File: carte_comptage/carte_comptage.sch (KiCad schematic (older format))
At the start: 34 parts, among them U3.3V MC33269ST-3.3T3G

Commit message: carte comptage SWD
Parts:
- added Rboot0: 100k, Resistor_SMD:R_1206_3216Metric, symbol Device:R
- added SWD: micromatch, TE_7-215079-6, symbol 7-215079-6:7-215079-6
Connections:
- net labels added: BOOT0, BUCK_EN, NRST, SWCLK, SWDIO, UART_RX, UART_TX
- net labels removed: boot0, buck_en, nrst
- wire segments 105 -> 107
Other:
- moved on the sheet: Cb1, Cb2, Cbbs, Cbc1, Cbc2, Cbdc1, Cbdc2, Cbdc3, Cbss, Cdc1, Cdc2, Cdc3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

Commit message: debut xtal a finir
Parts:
- added Dstatus1: LED, symbol Device:LED
- added Rstatus1: R, Resistor_SMD:R_1206_3216Metric, symbol Device:R
- SWD1: renamed from SWD; symbol 7-215079-6:7-215079-6 -> carte_comptage-rescue:7-215079-6-7-215079-6
- U3.3V1: renamed from U3.3V; symbol MC33269ST-3.3T3G:MC33269ST-3.3T3G -> carte_comptage-rescue:MC33269ST-3.3T3G-MC33269ST-3.3T3G
- USB1: renamed from USB; symbol USB4105-GF-A:USB4105-GF-A -> carte_comptage-rescue:USB4105-GF-A-USB4105-GF-A
- renumbered Cbbs to Cbbs1, Cbss to Cbss1, Cdcr to Cdcr1, Crst to Crst1, Db to Db1, Dpow to Dpow1, Dusb to Dusb1, F to F1, Jbat to Jbat1, Lb to Lb1, Rbc to Rbc1, RledP to RledP1, SWrst to SWrst1, buck to buck1, swBoot to swBoot1, µc to µc1
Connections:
- net labels added: LED_STATUS
- wire segments 107 -> 110
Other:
- moved on the sheet: Dpow1, RledP1

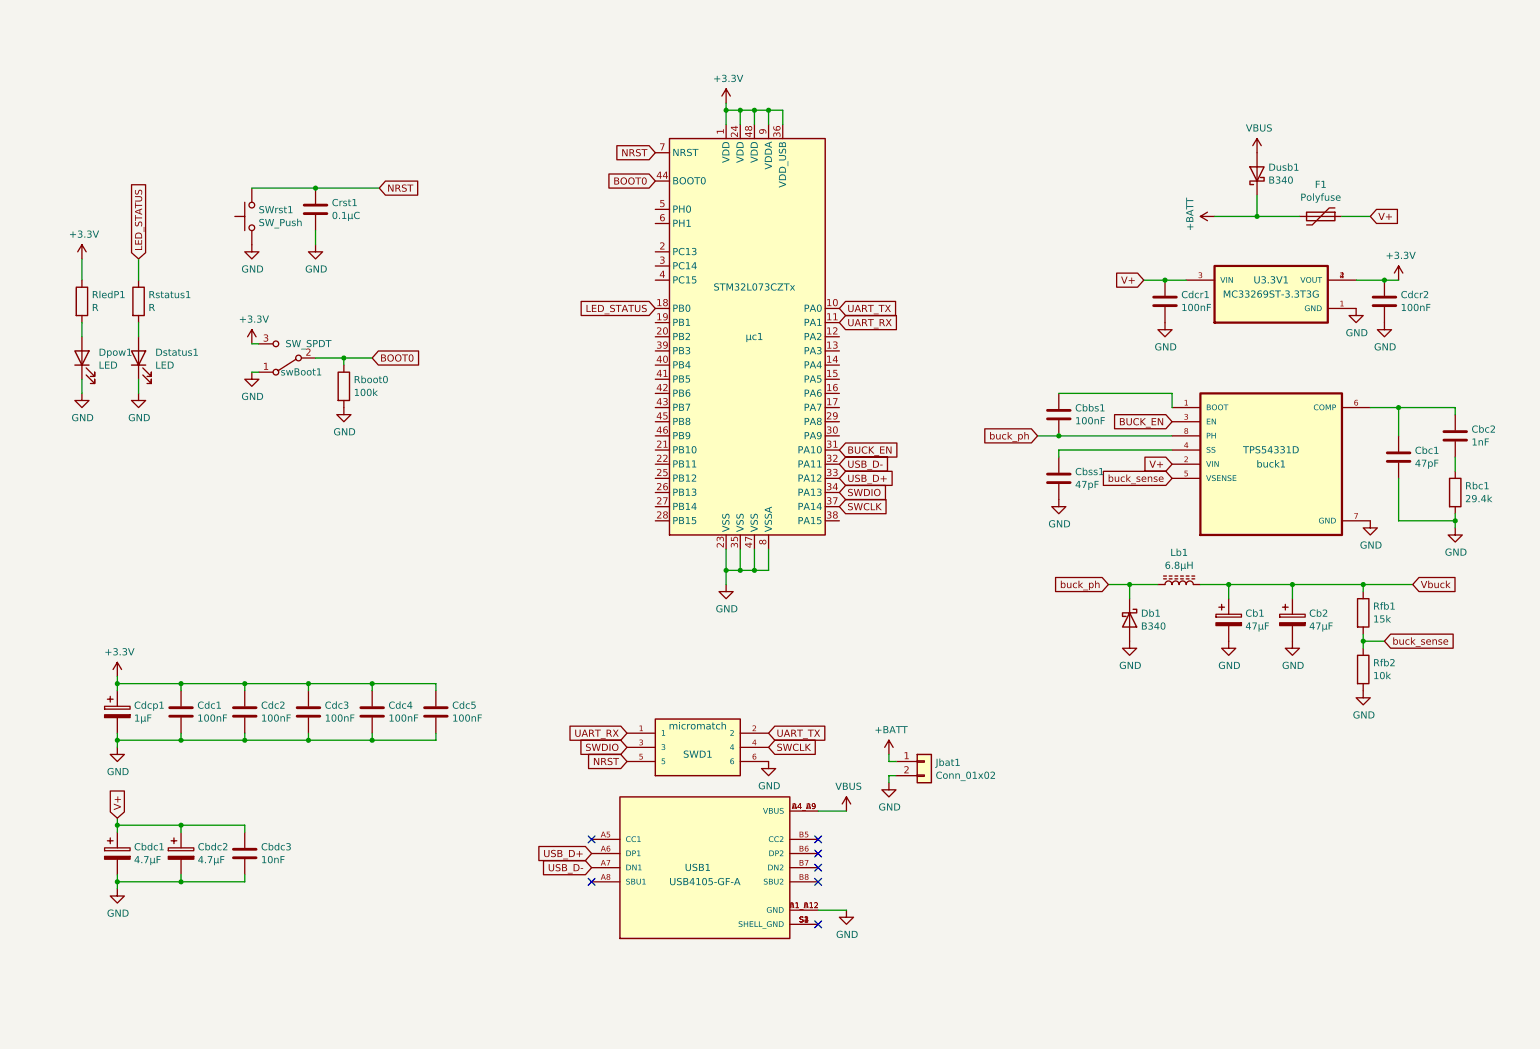
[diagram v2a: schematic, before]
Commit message: ajouté capteurs et réorganisé schéma
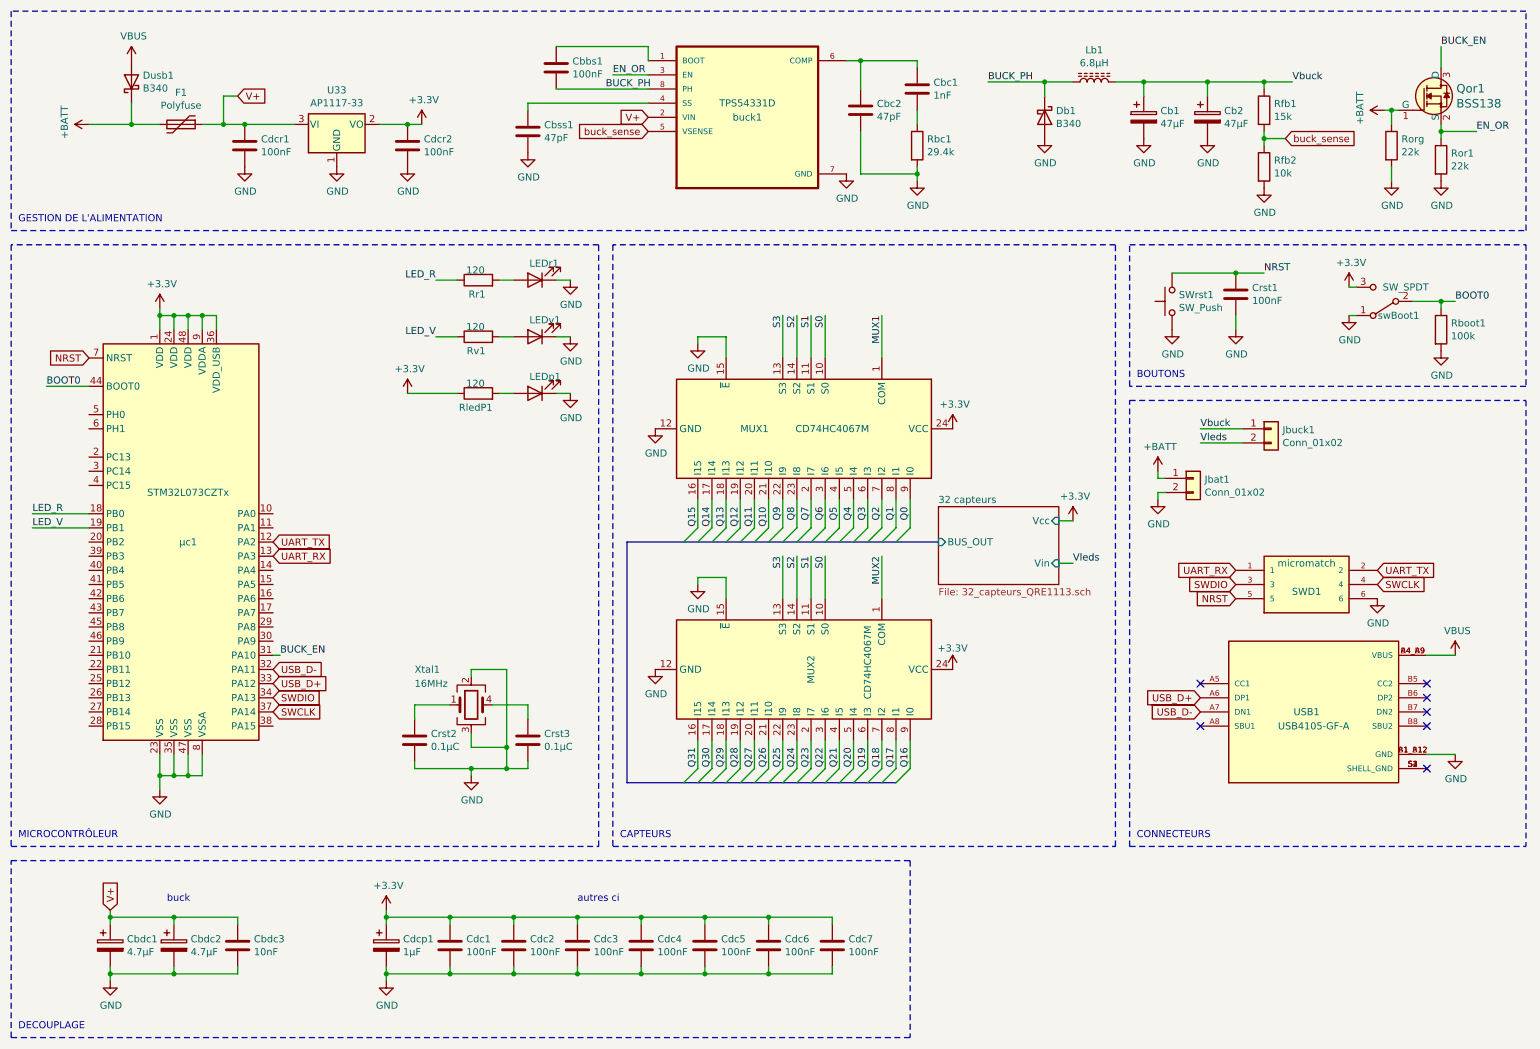
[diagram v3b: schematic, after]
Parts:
- removed U3.3V1: MC33269ST-3.3T3G, SOT230P700X175-4N, symbol carte_comptage-rescue:MC33269ST-3.3T3G-MC33269ST-3.3T3G
- added Cdc6, Cdc7: 100nF, symbol Device:C
- added Crst2, Crst3: 0.1µC, Capacitor_SMD:C_1206_3216Metric, symbol Device:C
- added Jbuck1: Conn_01x02, symbol Connector_Generic:Conn_01x02
- added LEDr1: LED, symbol Device:LED
- added MUX1, MUX2: CD74HC4067M, Package_SO:SOIC-24W_7.5x15.4mm_P1.27mm, symbol 74xx:CD74HC4067M
- added Qor1: BSS138, digikey-footprints:SOT-23-3, symbol dk_Transistors-FETs-MOSFETs-Single:BSS138
- added Ror1, Rorg: 22k, Resistor_SMD:R_1206_3216Metric, symbol Device:R
- added Rr1: 120, Resistor_SMD:R_1206_3216Metric, symbol Device:R
- added U33: AP1117-33, Package_TO_SOT_SMD:SOT-223-3_TabPin2, symbol Regulator_Linear:AP1117-33
- added Xtal1: 16MHz, symbol Device:Crystal_GND23
- Crst1: value 0.1µC -> 100nF
- RledP1: value R -> 120
- Rv1: renamed from Rstatus1; value R -> 120
- renumbered Cbc2 to Cbc1, Cbc1 to Cbc2, Dpow1 to LEDp1, Dstatus1 to LEDv1, Rboot0 to Rboot1
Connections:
- net +3V3: now also Cdc6.1, Cdc7.1, MUX1.24 (VCC), MUX2.24 (VCC), U33.2 (VO)
- net +BATT: now also Qor1.1 (G), Rorg.1
- net BUCK_EN: now also Qor1.3 (D); no longer buck1.3 (EN)
- net GND: now also Cdc6.2, Cdc7.2, Crst2.2, Crst3.2, LEDr1.1 (K), MUX1.12 (GND), MUX1.15 (~E), MUX2.12 (GND), MUX2.15 (~E), Ror1.2, Rorg.2, U33.1 (GND), Xtal1.2, Xtal1.3
- net UART_RX: now also µc1.13 (PA3); no longer µc1.11 (PA1)
- net UART_TX: now also µc1.12 (PA2); no longer µc1.10 (PA0)
- net V+: now also U33.3 (VI)
- net Vbuck: now also Jbuck1.1 (Pin_1)
- net LED_V: now reaches µc1.19 (PB1)
- net LED_V: now also Rv1.1
- net LED_STATUS renamed LED_R
- net LED_R: now also Rr1.1; no longer Rv1.1
- net buck_ph renamed BUCK_PH
- new net: Crst2.1, Xtal1.1
- new net: Crst3.1, Xtal1.4
- new net: LEDr1.2 (A), Rr1.2
- new net EN_OR: Qor1.2 (S), Ror1.1, buck1.3 (EN)
- new net MUX1: MUX1.1 (COM)
- new net MUX2: MUX2.1 (COM)
- new net Q0: MUX1.9 (I0)
- new net Q1: MUX1.8 (I1)
- new net Q10: MUX1.21 (I10)
- new net Q11: MUX1.20 (I11)
- new net Q12: MUX1.19 (I12)
- new net Q13: MUX1.18 (I13)
- new net Q14: MUX1.17 (I14)
- new net Q15: MUX1.16 (I15)
- new net Q16: MUX2.9 (I0)
- new net Q17: MUX2.8 (I1)
- new net Q18: MUX2.7 (I2)
- new net Q19: MUX2.6 (I3)
- new net Q2: MUX1.7 (I2)
- new net Q20: MUX2.5 (I4)
- new net Q21: MUX2.4 (I5)
- new net Q22: MUX2.3 (I6)
- new net Q23: MUX2.2 (I7)
- new net Q24: MUX2.23 (I8)
- new net Q25: MUX2.22 (I9)
- new net Q26: MUX2.21 (I10)
- new net Q27: MUX2.20 (I11)
- new net Q28: MUX2.19 (I12)
- new net Q29: MUX2.18 (I13)
- new net Q3: MUX1.6 (I3)
- new net Q30: MUX2.17 (I14)
- new net Q31: MUX2.16 (I15)
- new net Q4: MUX1.5 (I4)
- new net Q5: MUX1.4 (I5)
- new net Q6: MUX1.3 (I6)
- new net Q7: MUX1.2 (I7)
- new net Q8: MUX1.23 (I8)
- new net Q9: MUX1.22 (I9)
- new net S0: MUX1.10 (S0), MUX2.10 (S0)
- new net S1: MUX1.11 (S1), MUX2.11 (S1)
- new net S2: MUX1.14 (S2), MUX2.14 (S2)
- new net S3: MUX1.13 (S3), MUX2.13 (S3)
- new net Vleds: Jbuck1.2 (Pin_2)
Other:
- note added: "BOUTONS"
- note added: "CAPTEURS"
- note added: "CONNECTEURS"
- note added: "DECOUPLAGE"
- note added: "GESTION DE L'ALIMENTATION\n"
- note added: "MICROCONTRÔLEUR"
- note added: "autres ci"
- note added: "buck"
- moved on the sheet: Cb1, Cb2, Cbbs1, Cbc1, Cbc2, Cbdc1, Cbdc2, Cbdc3, Cbss1, Cdc1, Cdc2, Cdc3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

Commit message: projet cubeMX et connexions Xbee
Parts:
- added Dreverse: B340, Diode_SMD:D_SMC, symbol Diode:B340
- added JxbeeD, JxbeeG: Conn_01x10, symbol Connector_Generic:Conn_01x10
- added LoRa: B4B-XH-A(LF)(SN), JST_B4B-XH-A(LF)(SN), symbol B4B-XH-A_LF__SN_:B4B-XH-A(LF)(SN)
- Qor1: symbol dk_Transistors-FETs-MOSFETs-Single:BSS138 -> carte_comptage-rescue:BSS138-dk_Transistors-FETs-MOSFETs-Single
- renumbered Rorg to Rand1, Ror1 to Rand2
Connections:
- net +3V3: now also JxbeeG.1 (Pin_1), LoRa.4
- net GND: now also Dreverse.2 (A), JxbeeG.10 (Pin_10), LoRa.3
- net V+: now also Dreverse.1 (K)
- net LoRa_TX: now reaches µc1.10 (PA0)
- net LoRa_TX: now also LoRa.2
- net LoRa_RX: now reaches µc1.11 (PA1)
- net LoRa_RX: now also LoRa.1
- net XBEE_DIN: now reaches µc1.39 (PB3)
- net XBEE_DIN: now also JxbeeG.3 (Pin_3)
- net XBEE_DOUT: now reaches µc1.40 (PB4)
- net XBEE_DOUT: now also JxbeeG.2 (Pin_2)
- net EN_OR renamed EN_AND
- net buck_sense renamed BUCK_SENSE
- new net XBEE_ON_SLEEP: JxbeeD.3 (Pin_3)
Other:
- moved on the sheet: Cb1, Cb2, Cbbs1, Cbc1, Cbc2, Cbdc1, Cbdc2, Cbdc3, Cbss1, Cdcr1, Crst1, Crst2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

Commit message: Prêt à commencer le routage
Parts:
- removed RledP1, Rr1, Rv1: 120, Resistor_SMD:R_1206_3216Metric, symbol Device:R
- added Clse1, Clse2: 4pF, Capacitor_SMD:C_1206_3216Metric, symbol Device:C
- added J1: I2C, symbol Connector:Conn_01x03_Male
- added LSE1: 32.768MHz, symbol Device:Crystal
- added Rbat1: 113k, Resistor_SMD:R_1206_3216Metric, symbol Device:R_Small
- added Rbat2: 15k, Resistor_SMD:R_1206_3216Metric, symbol Device:R_Small
- added Rhse1, Rlse1: 220, Resistor_SMD:R_1206_3216Metric, symbol Device:R_Small
- added RledP1, Rr1, Rv1: 120, Resistor_SMD:R_1206_3216Metric, symbol Device:R_Small
- Cbbs1, Cbc1, Cbc2, Cbdc1, Cbdc2, Cbdc3, Cbss1, Cdc1, Cdc2, Cdc3, Cdc4, Cdc5, Cdc6, Cdc7, Cdcp1, Cdcr1, Cdcr2: footprint (none) -> Capacitor_SMD:C_1206_3216Metric
- Chse1: renamed from Crst2; value 0.1µC -> 100pF
- Chse2: renamed from Crst3; value 0.1µC -> 100pF
- JxbeeD1: renamed from JxbeeD; footprint (none) -> Connector_PinSocket_2.00mm:PinSocket_1x10_P2.00mm_Vertical
- JxbeeG1: renamed from JxbeeG; footprint (none) -> Connector_PinSocket_2.00mm:PinSocket_1x10_P2.00mm_Vertical
- LoRa1: renamed from LoRa; footprint JST_B4B-XH-A(LF)(SN) -> (none)
- SWD1: footprint TE_7-215079-6 -> (none)
- USB1: footprint GCT_USB4105-GF-A -> (none)
- buck1: footprint SOIC127P599X175-8N -> TPS54331D:SOIC127P599X175-8N
- renumbered Dreverse to Dreverse1
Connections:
- net +3V3: now also RledP1.1
- net GND: now also Clse1.2, Clse2.2, J1.3 (Pin_3), Rbat2.1
- net LED_R: now also µc1.14 (PA4), Rr1.1; no longer µc1.18 (PB0)
- net LED_V: now also µc1.15 (PA5), Rv1.1; no longer µc1.19 (PB1)
- net V+: now also Rbat1.2
- net SCL: now reaches µc1.21 (PB10)
- net SCL: now also J1.2 (Pin_2)
- net SDA: now reaches µc1.22 (PB11)
- net SDA: now also J1.1 (Pin_1)
- net LSE_IN: now reaches µc1.3 (PC14)
- net LSE_IN: now also Clse1.1, LSE1.1
- net LSE_OUT: now reaches µc1.4 (PC15)
- net LSE_OUT: now also Rlse1.1
- net HSE_IN: now reaches µc1.5 (PH0)
- net HSE_IN: now also Chse1.1, Xtal1.1
- net HSE_OUT: now reaches µc1.6 (PH1)
- net HSE_OUT: now also Rhse1.1
- net at LEDp1.2 (A): now also RledP1.2
- net at Chse2.1, Xtal1.4: now also Rhse1.2
- net at LEDv1.2 (A): now also Rv1.2
- net at LEDr1.2 (A): now also Rr1.2
- net XBEE_SLEEP: now reaches JxbeeG1.9 (Pin_9)
- net XBEE_ON_SLEEP renamed XBEE_SLEEPING
- new net: Clse2.1, LSE1.2, Rlse1.2
- new net BAT_SENSE: Rbat1.1, Rbat2.2, µc1.19 (PB1)
- no-connect marks 7 -> 38
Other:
- note added: "OSCILLATEURS"
- note added: "VOYANTS"
- moved on the sheet: Cbdc1, Cbdc2, Cbdc3, Cbss1, Cdc1, Cdc2, Cdc3, Cdc4, Cdc5, Cdc6, Cdc7, Cdcp1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
